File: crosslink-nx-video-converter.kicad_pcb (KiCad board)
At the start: 6 copper layers, 105.7 x 68 mm, 282 parts, among them J1 DC_SOCKET, J2 031-70526-21, J3 031-70526-21, J4 WE_68715014522_ONE-SIDE, J5 FTSH-105-01-F-DV-K, J6 WE_68715014522_ONE-SIDE, J7 2X05, J8 61300411121, Q1 2N7002, Q2 AO3401A, Q3 AO3401A, Q4 2N7002, Q5 AO3401A, Q6 2N7002, SW1 SW_DIP_x06, U1 MP20073, U10 AP7330-W5-7, U11 LIFCL-40-9BG256C, U12 MT41K128M16JT-125_K, U15 GS2971A, U16 GS2988, U17 SC18IS602BIPW, U18 W25Q32JVSSIQ, U2 LM339, U3 LM339, U5 AP62301WU-7, U6 AP62301WU-7, U7 AP62301WU-7, U8 AP7330-W5-7, U9 AP7330-W5-7, Y1 ABM7_27.000MH_D2Y_T, Y2 OSC40M-3.3_S5

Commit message: Routed hard CSI
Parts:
- U11: footprint crosslink-nx-video-converter-footprints:BGA-256_16x16_14.0x14.0mm -> antmicro-footprints:BGA-256_16x16_14.0x14.0mm
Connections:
- U11 pad A11: (no net) -> unconnected-(U11-PadA11)
- U11 pad A12: (no net) -> unconnected-(U11-PadA12)
- U11 pad A14: (no net) -> GND
- U11 pad A15: (no net) -> GND
- U11 pad A3: (no net) -> /Peripherals/MIPI1_D2_P
- U11 pad A4: (no net) -> /Peripherals/MIPI1_D0_P
- U11 pad A5: (no net) -> /Peripherals/MIPI1_CLK_P
- U11 pad A6: (no net) -> /Peripherals/MIPI1_D1_P
- U11 pad A7: (no net) -> /Peripherals/MIPI1_D3_P
- U11 pad A9: (no net) -> GND
- U11 pad B1: (no net) -> /Peripherals/MIPI0_D3_P
- U11 pad B12: (no net) -> unconnected-(U11-PadB12)
- U11 pad B16: (no net) -> /FPGA/DONE
- U11 pad B2: (no net) -> /Peripherals/MIPI0_D3_N
- U11 pad B3: (no net) -> /Peripherals/MIPI1_D2_N
- U11 pad B4: (no net) -> /Peripherals/MIPI1_D0_N
- U11 pad B5: (no net) -> /Peripherals/MIPI1_CLK_N
- U11 pad B6: (no net) -> /Peripherals/MIPI1_D1_N
- U11 pad B7: (no net) -> /Peripherals/MIPI1_D3_N
- U11 pad B9: (no net) -> GND
- U11 pad C1: (no net) -> /Peripherals/MIPI0_D1_P
- U11 pad C11: (no net) -> GND
- U11 pad C12: (no net) -> /FPGA/PROGRAMN
- U11 pad C13: (no net) -> unconnected-(U11-PadC13)
- U11 pad C14: (no net) -> /FPGA/SPI_DQ0_MOSI
- U11 pad C15: (no net) -> /FPGA/~{FLASH_CS}
- U11 pad C16: (no net) -> /FPGA/SPI_CLK
- U11 pad C2: (no net) -> /Peripherals/MIPI0_D1_N
- U11 pad D1: (no net) -> /Peripherals/MIPI0_CLK_P
- U11 pad D10: (no net) -> JTAG_EN
- U11 pad D11: (no net) -> /FPGA/INITN
- U11 pad D12: (no net) -> /FPGA/SPI_DQ3
- U11 pad D13: (no net) -> +3V3
- U11 pad D15: (no net) -> /FPGA/SPI_DQ2
- U11 pad D16: (no net) -> /FPGA/SPI_DQ1_MISO
- U11 pad D2: (no net) -> /Peripherals/MIPI0_CLK_N
- U11 pad D4: (no net) -> /SDI/RESET_TRST
- U11 pad D5: (no net) -> /SDI/STANDBY
- U11 pad D6: (no net) -> /SDI/SW_EN
- U11 pad E1: (no net) -> /Peripherals/MIPI0_D0_P
- U11 pad E10: (no net) -> /Peripherals/FFC2_VSYNC1
- U11 pad E11: (no net) -> TMS
- U11 pad E12: (no net) -> unconnected-(U11-PadE12)
- U11 pad E13: (no net) -> /Peripherals/FCC2_SDA2
- U11 pad E14: (no net) -> TDO
- U11 pad E15: (no net) -> LED0
- U11 pad E16: (no net) -> LED1
- U11 pad E2: (no net) -> /Peripherals/MIPI0_D0_N
- U11 pad E4: (no net) -> /SDI/~{CS_TMS}
- U11 pad E5: (no net) -> /SDI/SCLK_TCK
- U11 pad E6: (no net) -> /SDI/TIM_861
- U11 pad E9: (no net) -> /Peripherals/FFC2_RESET
- U11 pad F1: (no net) -> /Peripherals/MIPI0_D2_P
- U11 pad F10: (no net) -> /Peripherals/FFC1_RESET
- U11 pad F11: (no net) -> TDI
- U11 pad F13: (no net) -> +3V3
- U11 pad F14: (no net) -> TCK
- U11 pad F15: (no net) -> /Peripherals/FCC2_SCL2
- U11 pad F16: (no net) -> /Peripherals/FFC1_VSYNC0
- U11 pad F2: (no net) -> /Peripherals/MIPI0_D2_N
- U11 pad F4: (no net) -> /SDI/SDOUT_TDO
- U11 pad F5: (no net) -> +3V3
- U11 pad F6: (no net) -> /SDI/SDIN_TDI
- U11 pad F9: (no net) -> /Peripherals/FFC2_VSYNC0
- U11 pad G10: (no net) -> SCL
- U11 pad G11: (no net) -> /Peripherals/FCC1_SDA1
- U11 pad G12: (no net) -> /Peripherals/FCC1_SCL1
- U11 pad G13: (no net) -> /Peripherals/FCC1_SDA2
- U11 pad G14: (no net) -> /Peripherals/FCC1_SCL2
- U11 pad G15: (no net) -> 40MHz_3V3
- U11 pad G16: (no net) -> /Peripherals/FFC1_VSYNC1
- U11 pad G3: (no net) -> /SDI/SDI_STAT5
- U11 pad G4: (no net) -> /SDI/~{SDO_DISABLE}
- U11 pad G6: (no net) -> /SDI/SDO_EN/DIS
- U11 pad G9: (no net) -> SDA
- U11 pad H1: (no net) -> /SDI/SDI_D4
- U11 pad H2: (no net) -> /SDI/SDI_D5
- U11 pad H3: (no net) -> /SDI/SDI_D3
- U11 pad H4: (no net) -> /SDI/SDI_D2
- U11 pad H5: (no net) -> /SDI/SDI_D1
- U11 pad H6: (no net) -> /SDI/SDI_D0
- U11 pad J1: (no net) -> /SDI/SDI_D7
- U11 pad J2: (no net) -> /SDI/SDI_D8
- U11 pad J4: (no net) -> +3V3
- U11 pad J5: (no net) -> /SDI/SDI_D6
- U11 pad J6: (no net) -> /SDI/SDI_PCLK
- U11 pad K1: (no net) -> /SDI/SDI_D9
- U11 pad K2: (no net) -> /SDI/SDI_D10
- U11 pad K3: (no net) -> /SDI/SDI_D12
- U11 pad K4: (no net) -> /SDI/SDI_D11
- U11 pad K5: (no net) -> /SDI/SDI_D14
- U11 pad K6: (no net) -> /SDI/SDI_D13
- U11 pad L1: (no net) -> /SDI/SDI_D15
- U11 pad L2: (no net) -> /SDI/SDI_D16
- U11 pad L3: (no net) -> /SDI/SDI_STAT2
- U11 pad L4: (no net) -> /SDI/SDI_D19
- U11 pad L5: (no net) -> /SDI/SDI_STAT0
- U11 pad M1: (no net) -> /SDI/SDI_D17
- U11 pad M2: (no net) -> /SDI/SDI_D18
- U11 pad M3: (no net) -> /SDI/SDI_STAT1
- U11 pad N1: (no net) -> /SDI/SDI_STAT4
- U11 pad N2: (no net) -> /SDI/SDI_STAT3
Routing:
- net /Peripherals/MIPI2_D1_P: track 0.00 -> 51.4 mm, vias 0 -> 2
- net /Peripherals/MIPI2_D1_N: track 0.00 -> 51.0 mm, vias 0 -> 2
- net /Peripherals/MIPI2_CLK_N: track 0.00 -> 50.6 mm, vias 0 -> 2
- net /Peripherals/MIPI2_D3_N: track 1.56 -> 50.8 mm, vias 1 -> 2
- net /Peripherals/MIPI2_D3_P: track 1.39 -> 50.3 mm, vias 1 -> 2
- net /Peripherals/MIPI0_D3_N: track 0.00 -> 47.9 mm, vias 0 -> 2
- net /Peripherals/MIPI2_CLK_P: track 0.00 -> 47.9 mm, vias 0 -> 2
- net /Peripherals/MIPI0_CLK_N: track 0.00 -> 47.2 mm, vias 0 -> 2
- net /Peripherals/MIPI2_D0_P: track 0.00 -> 46.6 mm, vias 0 -> 2
- net /Peripherals/MIPI2_D0_N: track 0.00 -> 46.6 mm, vias 0 -> 2
- net /Peripherals/MIPI0_CLK_P: track 0.00 -> 46.4 mm, vias 0 -> 2
- net /Peripherals/MIPI0_D0_N: track 0.00 -> 45.2 mm, vias 0 -> 2
- net /Peripherals/MIPI0_D1_N: track 0.00 -> 44.8 mm, vias 0 -> 2
- net /Peripherals/MIPI0_D0_P: track 0.00 -> 44.3 mm, vias 0 -> 2
- net /Peripherals/MIPI0_D1_P: track 0.00 -> 43.8 mm, vias 0 -> 2
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- added copper zone on In6.Cu, net +1V2
- added copper zone on In5.Cu, net +1V5
- added copper zone on In6.Cu, net +1V5
- added copper zone on In6.Cu, net +3V3
- added copper zone on In6.Cu, net /FPGA Power/VCC_ADPHY
- added copper zone on In6.Cu, net /FPGA Power/VCC_AUX
- added copper zone on In6.Cu, net /FPGA Power/VCC_AUXA
- added copper zone on In6.Cu, net /FPGA Power/VCC_DPHY
- added copper zone on In6.Cu, net /FPGA Power/VCC_PLLDPHY
- added copper zone on In6.Cu, net 1V0_Power
- added copper zone on In3.Cu, net GND
- added copper zone on In5.Cu, net GND
- added copper zone on In6.Cu, net GND
- removed copper zone on In3.Cu, net +1V2
- removed copper zone on In3.Cu, net +1V5
- removed copper zone on In3.Cu, net +3V3
- removed copper zone on In3.Cu, net /FPGA Power/VCC_ADPHY
- removed copper zone on In3.Cu, net /FPGA Power/VCC_AUX
- removed copper zone on In3.Cu, net /FPGA Power/VCC_AUXA
- removed copper zone on In3.Cu, net /FPGA Power/VCC_DPHY
- removed copper zone on In3.Cu, net /FPGA Power/VCC_PLLDPHY
- removed copper zone on In3.Cu, net 1V0_Power
- removed copper zone on In3.Cu, net Vref
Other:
- copper layers 6 -> 8
- board text removed: "TODO: CHANGE INTERNAL TRACK WIDTH"

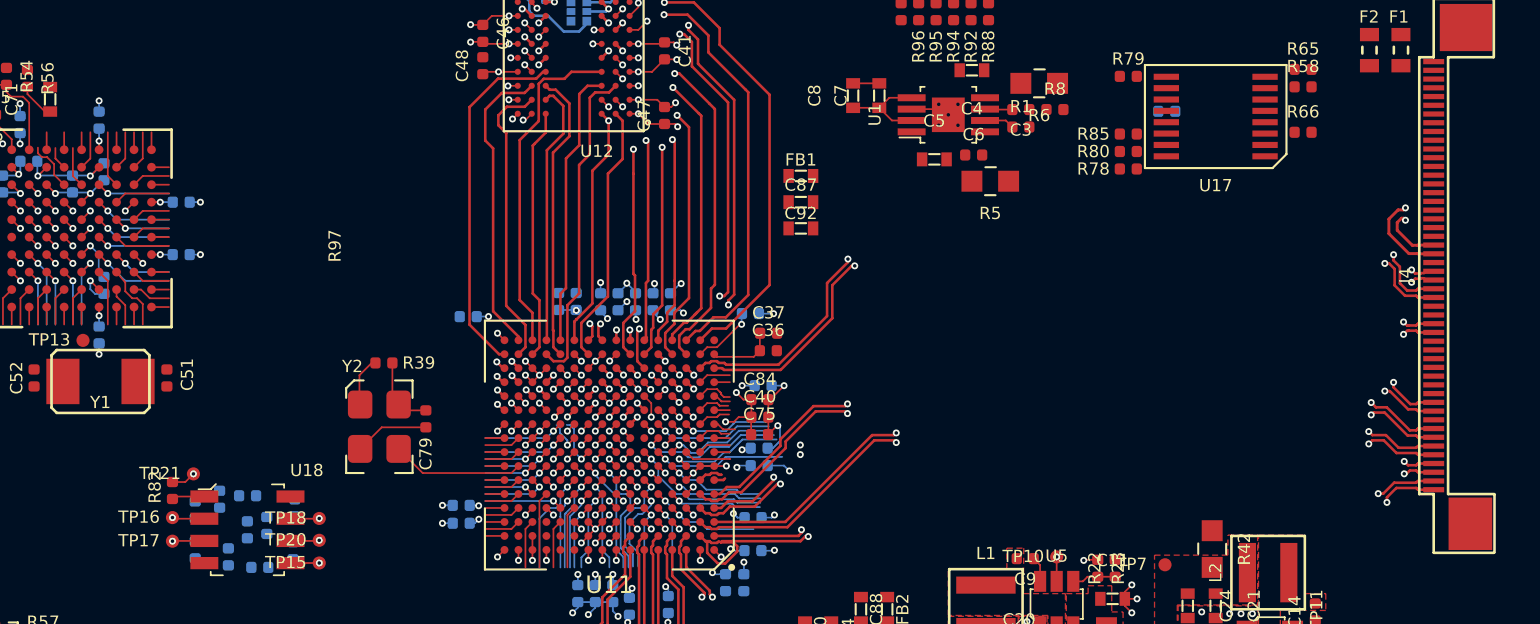
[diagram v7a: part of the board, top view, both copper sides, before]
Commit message: Routed SDI data interface
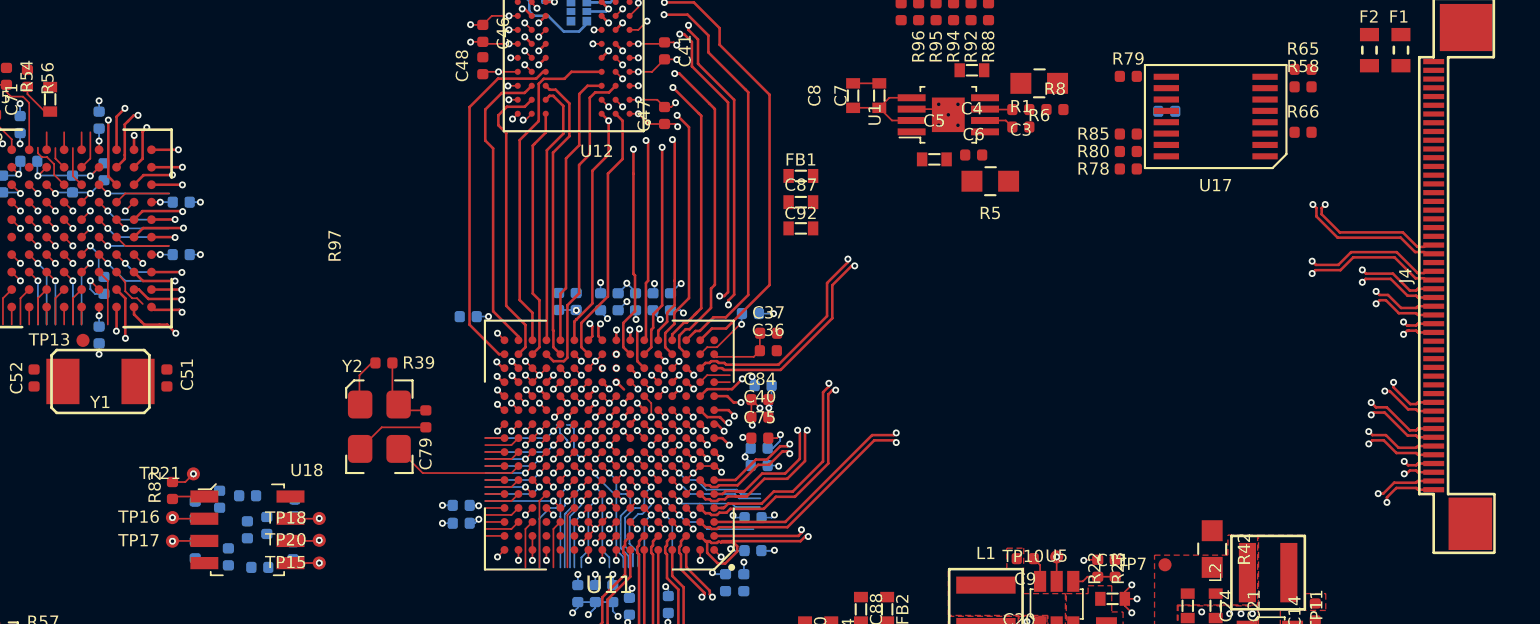
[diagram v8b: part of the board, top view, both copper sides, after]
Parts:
- moved C75 0.20 mm to (134.9, 89.9)
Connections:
- U11 pad H1: /SDI/SDI_D4 -> /SDI/SDI_D3
- U11 pad H2: /SDI/SDI_D5 -> /SDI/SDI_D14
- U11 pad H3: /SDI/SDI_D3 -> /SDI/SDI_D17
- U11 pad H4: /SDI/SDI_D2 -> /SDI/SDI_D8
- U11 pad H5: /SDI/SDI_D1 -> /SDI/SDI_D18
- U11 pad H6: /SDI/SDI_D0 -> /SDI/SDI_D12
- U11 pad J1: /SDI/SDI_D7 -> /SDI/SDI_D11
- U11 pad J2: /SDI/SDI_D8 -> /SDI/SDI_D4
- U11 pad J5: /SDI/SDI_D6 -> /SDI/SDI_D15
- U11 pad K1: /SDI/SDI_D9 -> /SDI/SDI_D2
- U11 pad K2: /SDI/SDI_D10 -> /SDI/SDI_D5
- U11 pad K3: /SDI/SDI_D12 -> /SDI/SDI_D7
- U11 pad K4: /SDI/SDI_D11 -> /SDI/SDI_D10
- U11 pad K5: /SDI/SDI_D14 -> /SDI/SDI_D13
- U11 pad K6: /SDI/SDI_D13 -> /SDI/SDI_D16
- U11 pad L1: /SDI/SDI_D15 -> /SDI/SDI_D0
- U11 pad L2: /SDI/SDI_D16 -> /SDI/SDI_D1
- U11 pad M1: /SDI/SDI_D17 -> /SDI/SDI_D9
- U11 pad M2: /SDI/SDI_D18 -> /SDI/SDI_D6
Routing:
- net /Peripherals/MIPI2_D2_N: track 6.85 -> 62.4 mm, vias 1 -> 2
- net /Peripherals/MIPI2_D2_P: track 7.29 -> 61.0 mm, vias 1 -> 2
- net /SDI/SDI_D9: track 2.32 -> 54.1 mm, vias 0 -> 2
- net /SDI/SDI_D6: track 10.6 -> 58.7 mm, vias 1 -> 2
- net /SDI/SDI_D11: track 1.57 -> 48.2 mm, vias 1 -> 2
- net /SDI/SDI_D0: track 9.17 -> 55.4 mm, vias 1 -> 2
- net /SDI/SDI_D1: track 9.86 -> 54.7 mm, vias 1 -> 2
- net /SDI/SDI_D17: track 2.02 -> 45.0 mm, vias 0 -> 2
- net /SDI/SDI_D18: track 3.09 -> 45.5 mm, vias 0 -> 2
- net /SDI/SDI_D19: track 2.77 -> 43.8 mm, vias 1 -> 2
- net /SDI/SDI_D4: track 3.11 -> 44.1 mm, vias 0 -> 2
- net /SDI/SDI_D2: track 7.60 -> 48.5 mm, vias 1 -> 2
- net /SDI/SDI_D12: track 8.19 -> 49.0 mm, vias 1 -> 2
- net /SDI/SDI_D3: track 3.67 -> 43.8 mm, vias 0 -> 2
- net /SDI/SDI_PCLK: track 1.00 -> 41.1 mm, vias 0 -> 2
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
